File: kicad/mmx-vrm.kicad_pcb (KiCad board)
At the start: 2 copper layers, 39.8 x 46.4 mm, 19 parts, among them J1 Conn_02x15_Row_Letter_First, SW1 SW_DIP_x03, U1 LM2596S, U2 LM2596S

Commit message: Revert "Renamed project into s7-vrm"
This reverts commit abb7c84a7e06dd52f3d76b1c246c1366ac80b644.
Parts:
- R3: value 9K -> 9.1K
- R5: value 2.9K -> 3K
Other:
- board text added: "MMX-VRM by Necroware"
- board text removed: "S7-VRM by Necroware"

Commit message: First raw version
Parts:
- removed D2: 1N5820, Diode_SMD:D_SMA
- removed L2: 47uH, Inductor_SMD:L_10.4x10.4_H4.8
- removed REF**: OSHW-Logo2_9.8x8mm_SilkScreen, Symbol:OSHW-Logo2_9.8x8mm_SilkScreen
- removed U2: LM2596S, Package_TO_SOT_SMD:TO-263-5_TabPin3
- added C4: 1mF, Capacitor_THT:CP_Radial_D6.3mm_P2.50mm, F.Cu at (133.3, 96.8)
- added C5: 1mF, Capacitor_THT:CP_Radial_D6.3mm_P2.50mm, F.Cu at (126.0, 96.8)
- added C6: 0.1u, Capacitor_SMD:C_1206_3216Metric_Pad1.33x1.80mm_HandSolder, F.Cu at (144.5, 95.8)
- added C7: 0.1u, Capacitor_SMD:C_1206_3216Metric_Pad1.33x1.80mm_HandSolder, F.Cu at (138.4, 69.8)
- added C8: C, Capacitor_SMD:C_1206_3216Metric_Pad1.33x1.80mm_HandSolder, F.Cu at (143.5, 71.8)
- added C9: C, Capacitor_SMD:C_1206_3216Metric_Pad1.33x1.80mm_HandSolder, F.Cu at (148.6, 71.8)
- added Q1: Q_NMOS_GDS, Package_TO_SOT_SMD:TO-252-2, F.Cu at (125.5, 70.5)
- added Q2: Q_NMOS_GDS, Package_TO_SOT_SMD:TO-252-2, F.Cu at (125.5, 78.1)
- added Q3: Q_NPN_BCE, Package_TO_SOT_SMD:SOT-23, F.Cu at (147.1, 90.7)
- added R8: 1K, Resistor_SMD:R_1206_3216Metric_Pad1.30x1.75mm_HandSolder, F.Cu at (144.5, 100.8)
- added R9: R, Resistor_SMD:R_1206_3216Metric_Pad1.30x1.75mm_HandSolder, F.Cu at (146.1, 71.8)
- C1, C2: value 820u -> 1mF; footprint Capacitor_THT:CP_Radial_D10.0mm_P5.00mm -> Capacitor_THT:CP_Radial_D6.3mm_P2.50mm
- C3: value 10nF -> 0.1u; moved to F.Cu
- D1: value 1N5820 -> D; footprint Diode_SMD:D_SMA -> Diode_SMD:D_1206_3216Metric_Pad1.42x1.75mm_HandSolder; moved to F.Cu
- R1: value 0 -> 1K
- R2: value 1K -> 3K; moved to F.Cu
- R3: value 9.1K -> 21K; moved to F.Cu
- R4: value 6.3K -> 15K; moved to F.Cu
- R5: value 3K -> 6,3K; moved to F.Cu
- R6: value 1.6K -> 3K; moved to F.Cu
- R7: value 1K -> 0; moved to F.Cu
- SW1: footprint Button_Switch_THT:SW_DIP_SPSTx03_Slide_9.78x9.8mm_W7.62mm_P2.54mm -> Button_Switch_THT:SW_DIP_SPSTx04_Slide_9.78x12.34mm_W7.62mm_P2.54mm
- U1: value LM2596S -> NCP1579; footprint Package_TO_SOT_SMD:TO-263-5_TabPin3 -> Package_SO:SOIC-8_3.9x4.9mm_P1.27mm
- moved D1 37.4 mm to (151.1, 71.8), turned to 270 degrees
- moved R7 25.1 mm to (144.5, 98.3), turned to 180 degrees
- moved C2 22.2 mm to (153.7, 86.4), turned to 180 degrees
- moved R6 21.9 mm to (141.2, 90.8), turned to 90 degrees
- moved C1 21.3 mm to (153.7, 94.0), turned to 180 degrees
- moved C3 20.5 mm to (145.1, 75.9), turned to 0 degrees
- moved R3 20.3 mm to (133.6, 90.8)
- moved R4 20.3 mm to (136.1, 90.8)
- moved R5 20.3 mm to (138.7, 90.8)
- moved R1 19.2 mm to (147.8, 80.3), turned to 270 degrees
- moved U1 18.4 mm to (138.4, 74.0), turned to 0 degrees
- moved SW1 13.2 mm to (135.9, 86.4)
- moved R2 8.01 mm to (143.8, 90.8), turned to 90 degrees
- moved J1 6.74 mm to (120.7, 102.9)
- moved L1 5.72 mm to (125.7, 88.9)
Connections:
- C1 pad 1: VCORE -> +5V
- C3 pad 1: VCORE -> +5V
- C3 pad 2: FB -> GND
- D1 pad 1: Net-(D1-Pad1) -> Net-(C7-Pad1)
- D1 pad 2: GND -> +5V
- J1 pad a9: GND -> (no net)
- L1 pad 1: Net-(D1-Pad1) -> Net-(C7-Pad2)
- R1 pad 1: SENSE -> FB
- R1 pad 2: VCORE -> GND
- R2 pad 1: PWRGOOD -> VCORE
- R2 pad 2: VCORE -> FB
- R6 pad 2: FB -> Net-(R6-Pad2)
- R7 pad 1: FB -> SENSE
- R7 pad 2: GND -> VCORE
- SW1 pad 1: FB -> Net-(R3-Pad2)
- SW1 pad 2: FB -> Net-(R4-Pad2)
- SW1 pad 3: FB -> Net-(R5-Pad2)
- SW1 pad 4: Net-(R5-Pad2) -> Net-(R6-Pad2)
- SW1 pad 5: Net-(R4-Pad2) -> FB
- SW1 pad 6: Net-(R3-Pad2) -> FB
- U1 pad 1: +5V -> Net-(C7-Pad1)
- U1 pad 2: Net-(D1-Pad1) -> Net-(Q1-Pad1)
- U1 pad 4: FB -> Net-(Q2-Pad1)
- U1 pad 5: DISABLE -> +5V
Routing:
- net DISABLE: track 50.5 -> 16.0 mm, vias 2 -> 1
- net VCORE: track 27.6 -> 0.00 mm, vias 4 -> 9
- net GND: track 27.1 -> 2.40 mm, vias 34 -> 5
- net Net-(C7-Pad2): track 0.00 -> 23.7 mm, vias 0 -> 2
- net Net-(C8-Pad1): track 0.00 -> 22.6 mm, vias 0 -> 2
- net Net-(C7-Pad1): track 0.00 -> 18.3 mm
- net +5V: track 0.00 -> 7.56 mm, vias 21 -> 37
- net Net-(D2-Pad1): track 6.38 -> 0.00 mm, vias 1 -> 0
- net Net-(D1-Pad1): track 5.45 -> 0.00 mm, vias 1 -> 0
- net FB: track 32.8 -> 37.8 mm, vias 2 -> 0
- net Net-(R6-Pad2): track 0.00 -> 3.84 mm
- net SENSE: track 4.47 -> 8.15 mm
- net Net-(C9-Pad1): track 0.00 -> 2.55 mm
- net Net-(R5-Pad2): track 2.30 -> 3.84 mm
- net Net-(R4-Pad2): track 2.30 -> 3.84 mm
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- added copper zone on F.Cu, net Net-(C7-Pad2)
- added copper zone on F.Cu, net Net-(Q1-Pad1)
- added copper zone on F.Cu, net Net-(Q2-Pad1)
- removed copper zone on F.Cu, net Net-(D1-Pad1)
- removed copper zone on F.Cu, net Net-(D2-Pad1)
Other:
- board size 39.8 x 46.4 mm -> 39.4 x 42.9 mm
- net class Power added: clearance 0.2, trace_width 1, via_dia 0.8, via_drill 0.4
- board text removed: "1"
- board text removed: "15"
- board text removed: "MMX-VRM by Necroware"
- board text removed: "SW1 Settings: 000: 3.2V 100: 2.9V 010: 2.8V 110: 2.6V 001: 2.5V 101: 2.4V 011: 2.3V 111: 2.2V"
- board text removed: "rev 0.2"

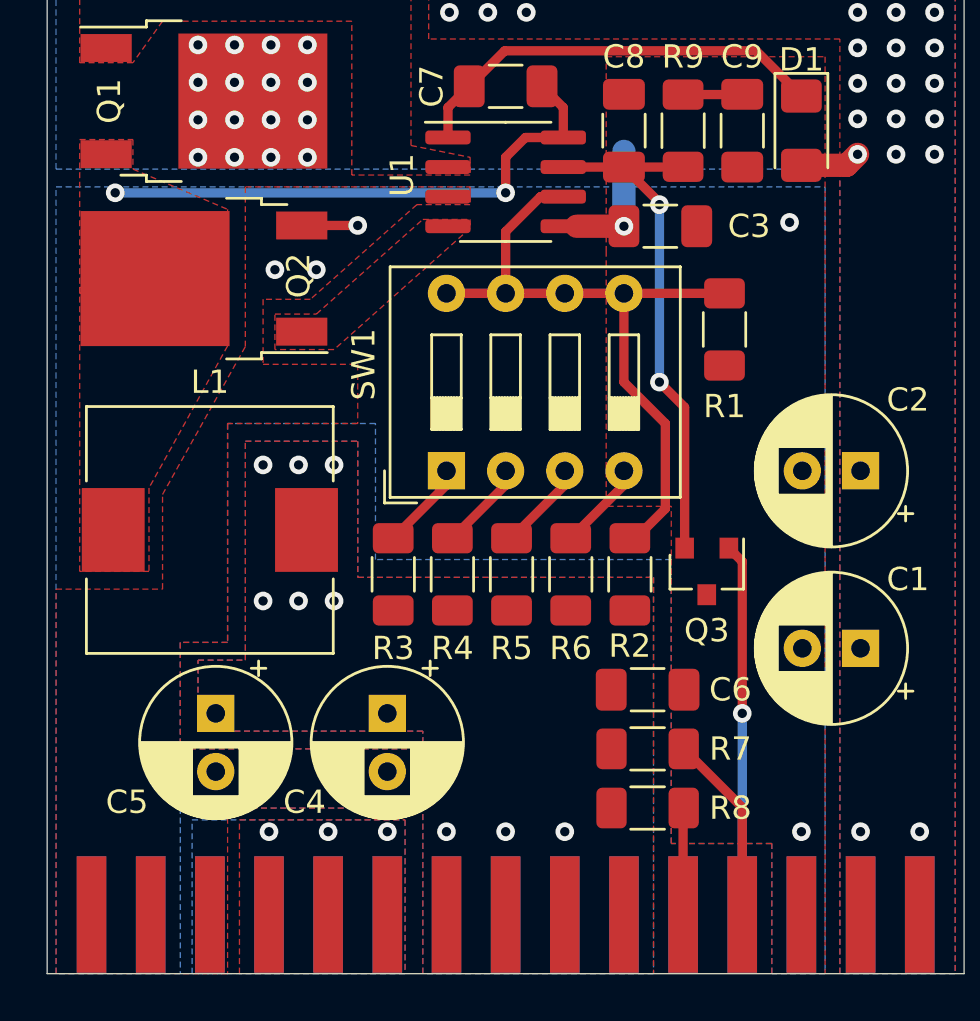
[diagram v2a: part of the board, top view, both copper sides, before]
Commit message: Improved power lines
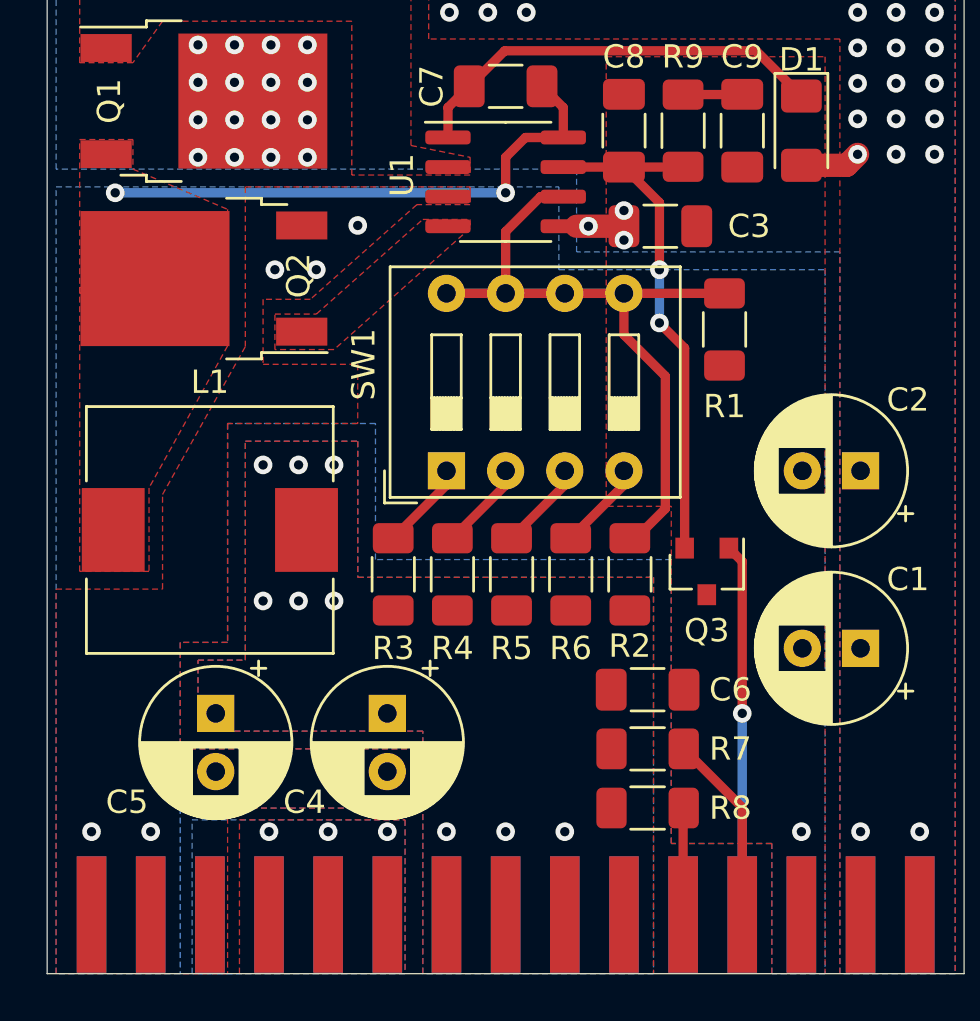
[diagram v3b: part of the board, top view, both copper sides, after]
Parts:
- added REF**: OSHW-Logo2_9.8x8mm_SilkScreen, Symbol:OSHW-Logo2_9.8x8mm_SilkScreen, F.Cu at (151.6, 78.5)
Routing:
- net +5V: track 7.56 -> 4.35 mm, vias 37 -> 39
- net GND: track 2.40 -> 0.00 mm, vias 5 -> 6
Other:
- board text added: "MMX-VRM by Necroware"
- board text added: "SW1 Settings: 0000: 3.2V 1000: 2.9V 0100: 2.8V 1100: 2.6V 0010: 2.4V 1010: 2.3V 0110: 2.2V 1110: 2.1V 0001: 2.0V 1001: 1.9V 1101: 1.8V 0111: 1.7V 1111: 1.6V"
- board text added: "rev 0.3"

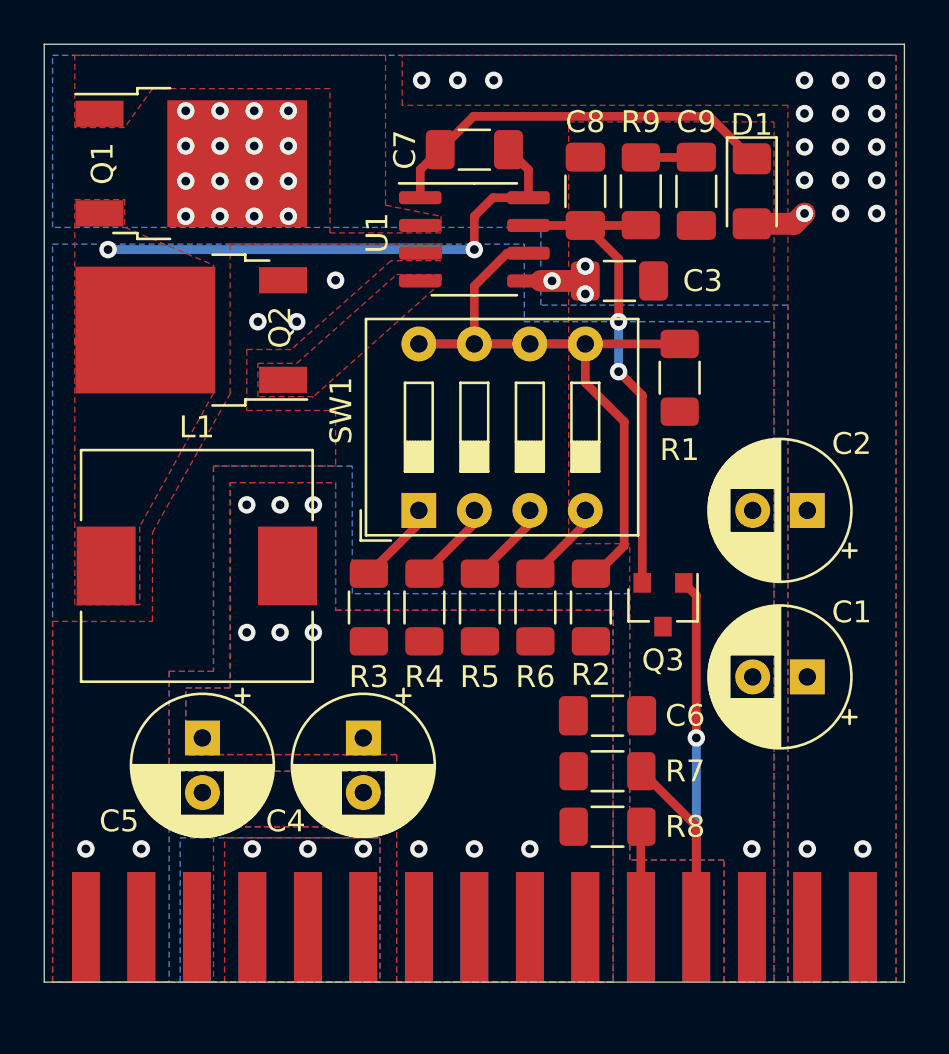
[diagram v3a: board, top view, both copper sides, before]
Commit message: Add LCSC IDs and documentation
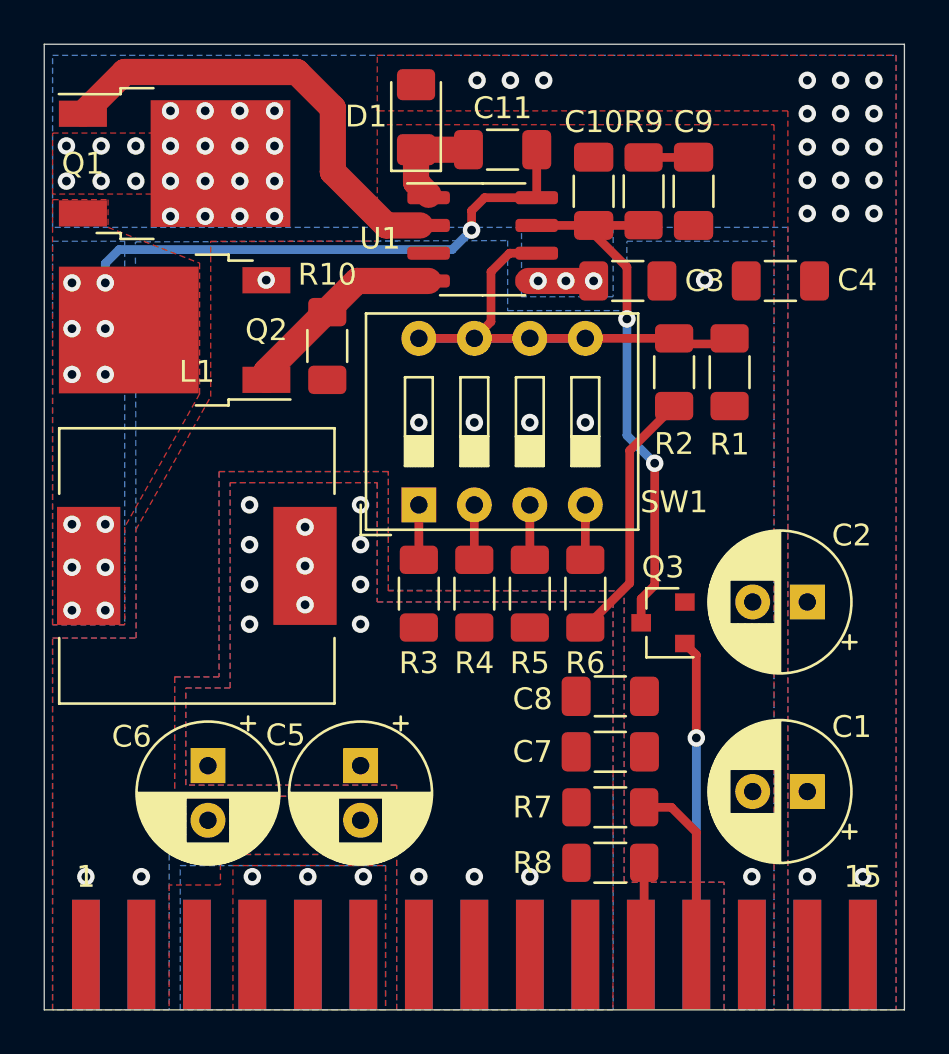
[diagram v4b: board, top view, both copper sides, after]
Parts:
- removed the C6 at (144.5, 95.8)
- added C5: 1mF, Capacitor_THT:CP_Radial_D6.3mm_P2.50mm, F.Cu at (133.2, 98.0)
- added C7: 4.7u, Capacitor_SMD:C_1206_3216Metric_Pad1.33x1.80mm_HandSolder, F.Cu at (144.7, 97.4)
- added C8: 0.1u, Capacitor_SMD:C_1206_3216Metric_Pad1.33x1.80mm_HandSolder, F.Cu at (144.7, 94.9)
- added R10: 15K, Resistor_SMD:R_1206_3216Metric_Pad1.30x1.75mm_HandSolder, F.Cu at (131.7, 78.8)
- C10: renamed from C8; value C -> 386p
- C4: value 1mF -> 4.7u; footprint Capacitor_THT:CP_Radial_D6.3mm_P2.50mm -> Capacitor_SMD:C_1206_3216Metric_Pad1.33x1.80mm_HandSolder
- C9: value C -> 81n
- L1: value 47uH -> 1,2uH; footprint Inductor_SMD:L_10.4x10.4_H4.8 -> Inductor_SMD:L_12x12mm_H4.5mm
- Q3: value Q_NPN_BCE -> Q_NPN_BEC
- R9: value R -> 3K
- SW1: value SW_DIP_x03 -> SW_DIP_x04
- moved C4 28.3 mm to (152.4, 75.9), turned to 180 degrees
- moved D1 15.7 mm to (135.8, 68.4), turned to 90 degrees
- moved R2 11.4 mm to (147.6, 80.0)
- moved C1 5.25 mm to (153.7, 99.2)
- moved C2 4.19 mm to (153.7, 90.6)
- moved R4 2.37 mm to (138.4, 90.2)
- moved R5 2.37 mm to (141.0, 90.2)
- moved R6 2.37 mm to (143.5, 90.2)
- moved R3 2.37 mm to (135.9, 90.2)
- moved R1 2.30 mm to (150.1, 80.0)
- moved R8 1.66 mm to (144.7, 102.5)
- moved R7 1.66 mm to (144.7, 99.9)
- moved C6 1.30 mm to (126.2, 98.0)
- moved C11 1.29 mm to (139.7, 69.8)
- moved J1 1.27 mm to (120.7, 104.1)
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- renumbered C7 to C11, C5 to C6
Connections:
- C10 pad 1: Net-(C8-Pad1) -> Net-(C10-Pad1)
- C4 pad 1: VCORE -> +5V
- Q3 pad 2: Net-(C8-Pad1) -> GND
- Q3 pad 3: GND -> Net-(C10-Pad1)
- R9 pad 1: Net-(C8-Pad1) -> Net-(C10-Pad1)
- U1 pad 7: Net-(C8-Pad1) -> Net-(C10-Pad1)
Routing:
- net Net-(C10-Pad1): track 0.00 -> 24.7 mm, vias 0 -> 2
- net Net-(C8-Pad1): track 22.6 -> 0.00 mm, vias 2 -> 0
- net Net-(Q1-Pad1): track 0.00 -> 20.9 mm
- net Net-(C11-Pad1): track 18.3 -> 4.70 mm
- net VCORE: track 0.00 -> 11.8 mm, vias 9 -> 14
- net FB: track 37.8 -> 27.7 mm
- net Net-(Q2-Pad1): track 0.97 -> 9.52 mm
- net DISABLE: track 16.0 -> 13.2 mm
- net +5V: track 4.35 -> 2.31 mm, vias 39 -> 45
- net Net-(R5-Pad2): track 3.84 -> 2.51 mm
- net Net-(R4-Pad2): track 3.84 -> 2.51 mm
- net Net-(R3-Pad2): track 3.84 -> 2.51 mm
- net Net-(R6-Pad2): track 3.84 -> 3.02 mm
- net Net-(C11-Pad2): track 23.7 -> 24.2 mm, vias 2 -> 13
- net GND: vias 6 -> 9
- added copper zone on B.Cu, net Net-(C11-Pad2)
- removed copper zone on F.Cu, net Net-(Q1-Pad1)
- removed copper zone on F.Cu, net Net-(Q2-Pad1)
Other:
- board size 39.4 x 42.9 mm -> 39.4 x 44.2 mm
- net class Power: trace_width 1 -> 1.2
- board text added: "1"
- board text added: "15"

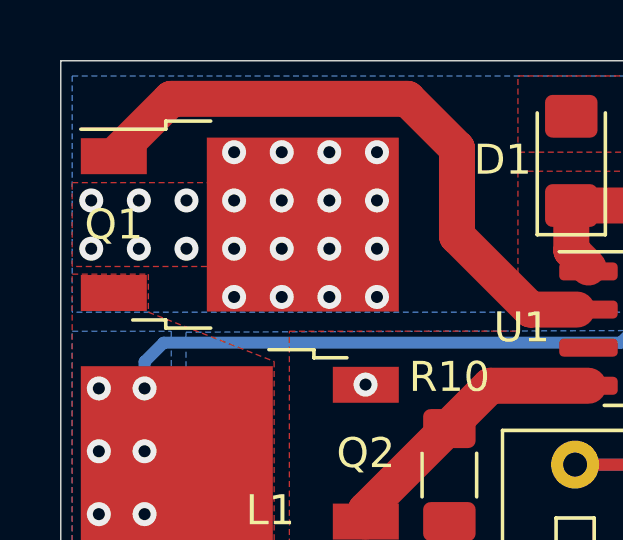
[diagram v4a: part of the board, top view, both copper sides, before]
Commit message: Minor fixes.
- Changed LCSC part numbers (due to shortage)
- Enlarged GND plane distance
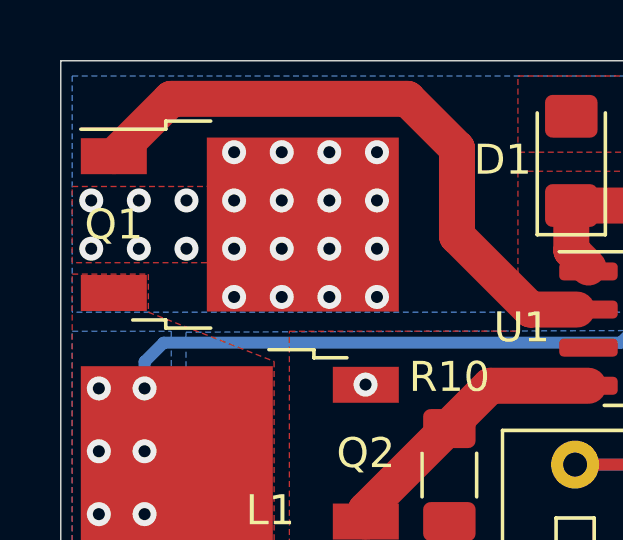
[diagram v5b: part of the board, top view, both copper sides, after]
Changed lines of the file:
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@@
     (last_trace_width 0.4)
     (trace_clearance 0.2)
-    (zone_clearance 0.254)
+    (zone_clearance 0.4)
     (zone_45_only no)
     (trace_min 0.2)
@@
       (drillshape 0)
       (scaleselection 1)
-      (outputdirectory "./gerber"))
+      (outputdirectory "gerber"))
   )
   (net 0 "")
@@
     (add_net FB)
     (add_net "Net-(C10-Pad1)")
-    (add_net "Net-(C11-Pad1)")
     (add_net "Net-(C11-Pad2)")
     (add_net "Net-(C9-Pad1)")
@@
     (add_net +5V)
     (add_net GND)
+    (add_net "Net-(C11-Pad1)")
     (add_net "Net-(Q1-Pad1)")
     (add_net "Net-(Q2-Pad1)")
@@
   (gr_line (start 158.115 109.22) (end 158.115 65.024) (layer Edge.Cuts) (width 0.05))
   (gr_line (start 118.745 109.22) (end 158.115 109.22) (layer Edge.Cuts) (width 0.05))
-  (via blind (at 120.014996 90.932) (size 0.8) (drill 0.4) (layers F.Cu B.Cu) (net 17))
-  (via blind (at 121.539 90.932) (size 0.8) (drill 0.4) (layers F.Cu B.Cu) (net 17))
-  (via blind (at 121.539 80.137) (size 0.8) (drill 0.4) (layers F.Cu B.Cu) (net 17))
-  (via blind (at 120.014996 80.137) (size 0.8) (drill 0.4) (layers F.Cu B.Cu) (net 17))
-  (via blind (at 121.539 86.995) (size 0.8) (drill 0.4) (layers F.Cu B.Cu) (net 17))
-  (via blind (at 120.014996 86.995) (size 0.8) (drill 0.4) (layers F.Cu B.Cu) (net 17))
-  (via blind (at 130.683 87.122) (size 0.8) (drill 0.4) (layers F.Cu B.Cu) (net 3))
-  (via blind (at 130.683 88.9) (size 0.8) (drill 0.4) (layers F.Cu B.Cu) (net 3))
-  (via blind (at 130.683 90.678) (size 0.8) (drill 0.4) (layers F.Cu B.Cu) (net 3))
   (via blind (at 128.905 75.819) (size 0.8) (drill 0.4) (layers F.Cu B.Cu) (net 1))
   (via blind (at 138.43 82.3385) (size 0.8) (drill 0.4) (layers F.Cu B.Cu) (net 1))
@@
   (segment (start 140.905 75.8575) (end 143.2175 75.8575) (width 1.2) (layer F.Cu) (net 2))
   (via blind (at 153.67 72.771) (size 0.8) (drill 0.4) (layers F.Cu B.Cu) (net 2))
+  (via blind (at 130.683 87.122) (size 0.8) (drill 0.4) (layers F.Cu B.Cu) (net 3))
+  (via blind (at 130.683 88.9) (size 0.8) (drill 0.4) (layers F.Cu B.Cu) (net 3))
+  (via blind (at 130.683 90.678) (size 0.8) (drill 0.4) (layers F.Cu B.Cu) (net 3))
   (via blind (at 133.223 87.926333) (size 0.8) (drill 0.4) (layers F.Cu B.Cu) (net 3))
   (via blind (at 133.223 86.106) (size 0.8) (drill 0.4) (layers F.Cu B.Cu) (net 3))
@@
   (segment (start 146.066 90.408) (end 146.685 89.789) (width 0.4) (layer F.Cu) (net 16))
   (segment (start 146.066 91.5035) (end 146.066 90.408) (width 0.4) (layer F.Cu) (net 16))
+  (via blind (at 120.014996 90.932) (size 0.8) (drill 0.4) (layers F.Cu B.Cu) (net 17))
+  (via blind (at 121.539 90.932) (size 0.8) (drill 0.4) (layers F.Cu B.Cu) (net 17))
+  (via blind (at 121.539 80.137) (size 0.8) (drill 0.4) (layers F.Cu B.Cu) (net 17))
+  (via blind (at 120.014996 80.137) (size 0.8) (drill 0.4) (layers F.Cu B.Cu) (net 17))
+  (via blind (at 121.539 86.995) (size 0.8) (drill 0.4) (layers F.Cu B.Cu) (net 17))
+  (via blind (at 120.014996 86.995) (size 0.8) (drill 0.4) (layers F.Cu B.Cu) (net 17))
   (via blind (at 121.539 88.9635) (size 0.8) (drill 0.4) (layers F.Cu B.Cu) (net 17))
   (via blind (at 120.014996 88.9635) (size 0.8) (drill 0.4) (layers F.Cu B.Cu) (net 17))
@@
   )
   (zone (net 1) (net_name GND) (layer F.Cu) (hatch edge 0.508)
-    (connect_pads (clearance 0.254))
+    (connect_pads (clearance 0.4))
     (min_thickness 0.254)
     (fill yes (arc_segments 32) (thermal_gap 0.254) (thermal_bridge_width 1))
@@
     (polygon
       (pts
-        (xy 125.857 71.882) (xy 119.126 71.882) (xy 119.126 69.088) (xy 125.857 69.088)
+        (xy 125.857 71.755) (xy 119.126 71.755) (xy 119.126 69.215) (xy 125.857 69.215)
       )
     )
